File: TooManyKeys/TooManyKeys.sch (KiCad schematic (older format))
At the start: 16 parts

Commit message: Matrix sch finished
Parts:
- R?: value 1k -> 10k
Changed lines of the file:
@@
 $Descr A4 11693 8268
 encoding utf-8
-Sheet 1 1
+Sheet 1 2
 Title ""
 Date ""
@@
 P 1550 3200
 F 0 "R?" V 1354 3200 50  0000 C CNN
-F 1 "1k" V 1445 3200 50  0000 C CNN
+F 1 "10k" V 1445 3200 50  0000 C CNN
 F 2 "" H 1550 3200 50  0001 C CNN
 F 3 "~" H 1550 3200 50  0001 C CNN
@@
 Wire Wire Line
 	2500 4900 2900 4900
+$Sheet
+S 1850 6650 1100 550
+U 5E8A6E89
+F0 "Matrix" 50
+F1 "Matrix.sch" 50
+$EndSheet
 $EndSCHEMATC

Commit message: adding voltage controller and i2c controller
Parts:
- removed F?: 500mA, symbol Device:Polyfuse
- removed USB?: Molex-0548190589, symbol random-keyboard-parts:Molex-0548190589
- added C? (x4): 1uF, Capacitors_SMD:C_0603, symbol Device:C_Small
- added C? (x3): 2.2uF, symbol Device:C_Small
- added C?: 10uF, symbol Device:C_Small
- added C?: 22uF, symbol Device:C_Small
- added F?: 500mA, symbol Device:Polyfuse
- added J?: 54104-3031_Oled, 5051103091, symbol SamacSys_Parts:505110-3091_Oled
- added R? (x2): 5.1k, symbol Device:R_Small
- added R?: 560K, symbol Device:R_Small
- added R? (x2): 4.7k, symbol Device:R_Small
- added R?: 200k, symbol Device:R_Small
- added U?: PRTR5V0U2X, symbol random-keyboard-parts:PRTR5V0U2X
- added U?: PCA9306, symbol Interface:PCA9306
- added U?: AP1117-33, Package_TO_SOT_SMD:SOT-223-3_TabPin2, symbol Regulator_Linear:AP1117-33
- added USB?: HRO-TYPE-C-31-M-12, symbol Type-C:HRO-TYPE-C-31-M-12
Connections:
- net labels added: +3.3V, COL00, COL01, COL02, COL03, COL04, COL05, COL06, COL07, COL08, COL09, COL10, COL11, COL12, COL13, COL14, COL15, COL16, COL17, COL18, COL19, COL20, COL21, COL22, COL23, LED, RESET, ROW0, ROW1, ROW2, ROW3, ROW4, ROW5, ROW6, ROW7, SCL, SCL_3.3, SDA, SDA_3.3
- wire segments 43 -> 166
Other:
- moved on the sheet: C?, R?, SW?, Y?

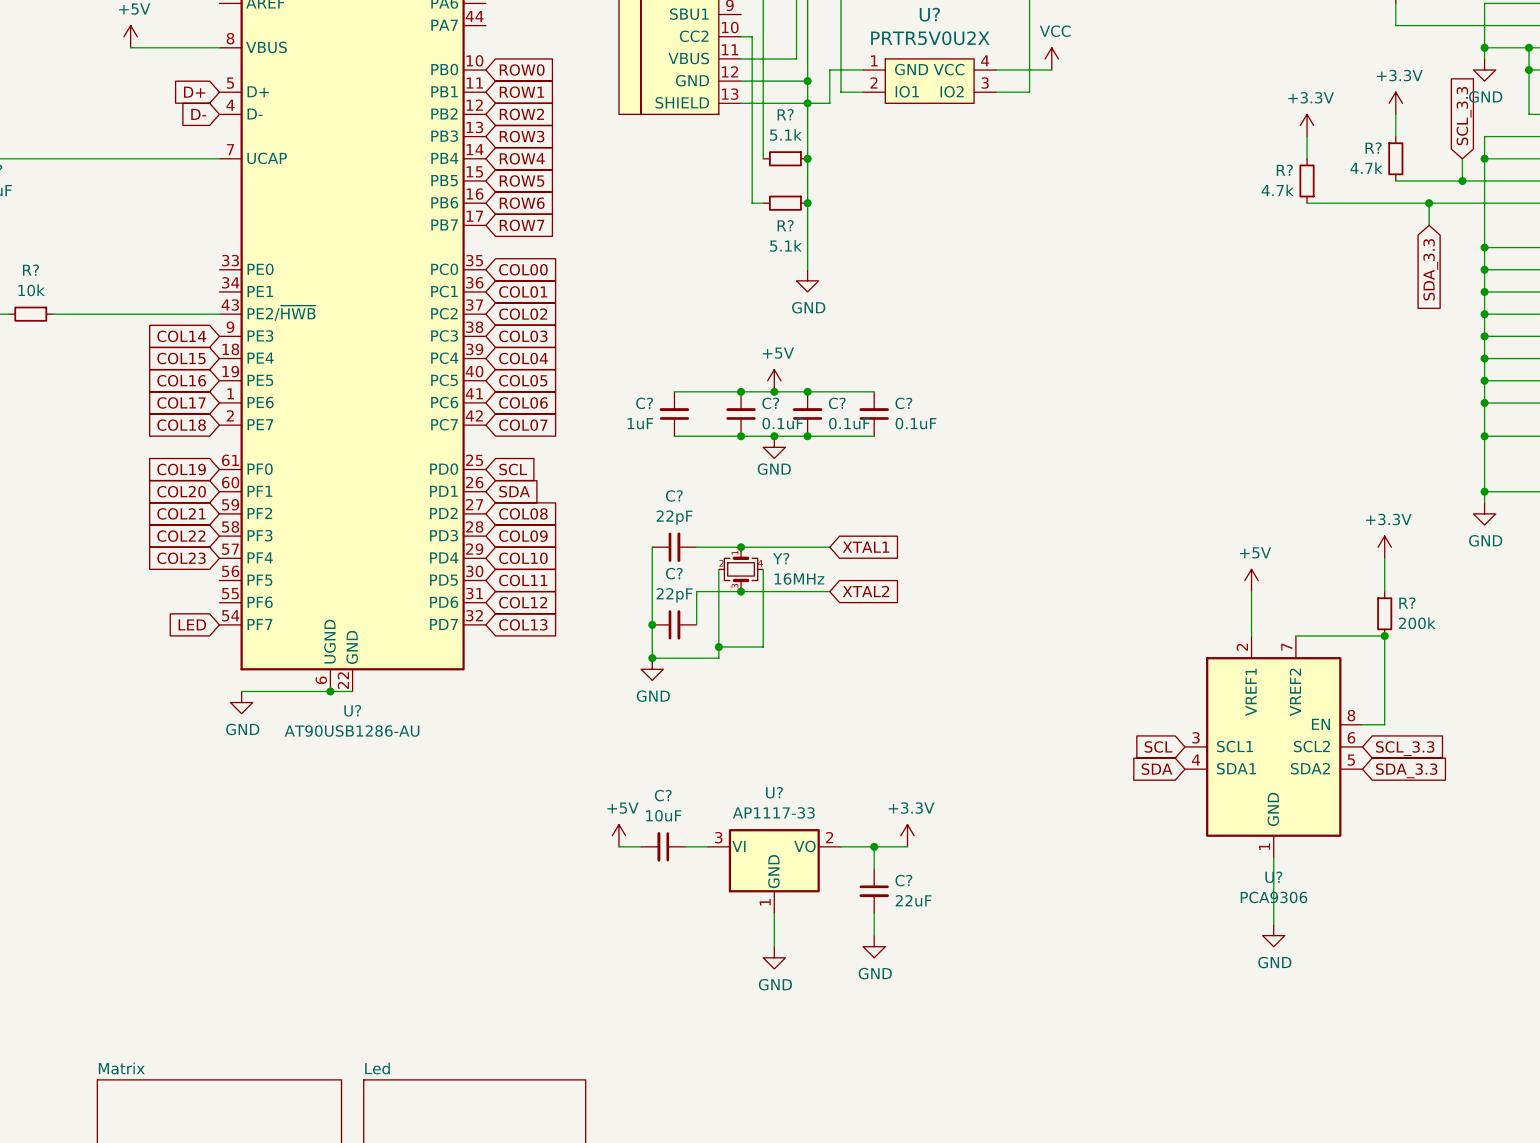
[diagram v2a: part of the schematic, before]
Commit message: adding IS31FL3733-TQ to led sch
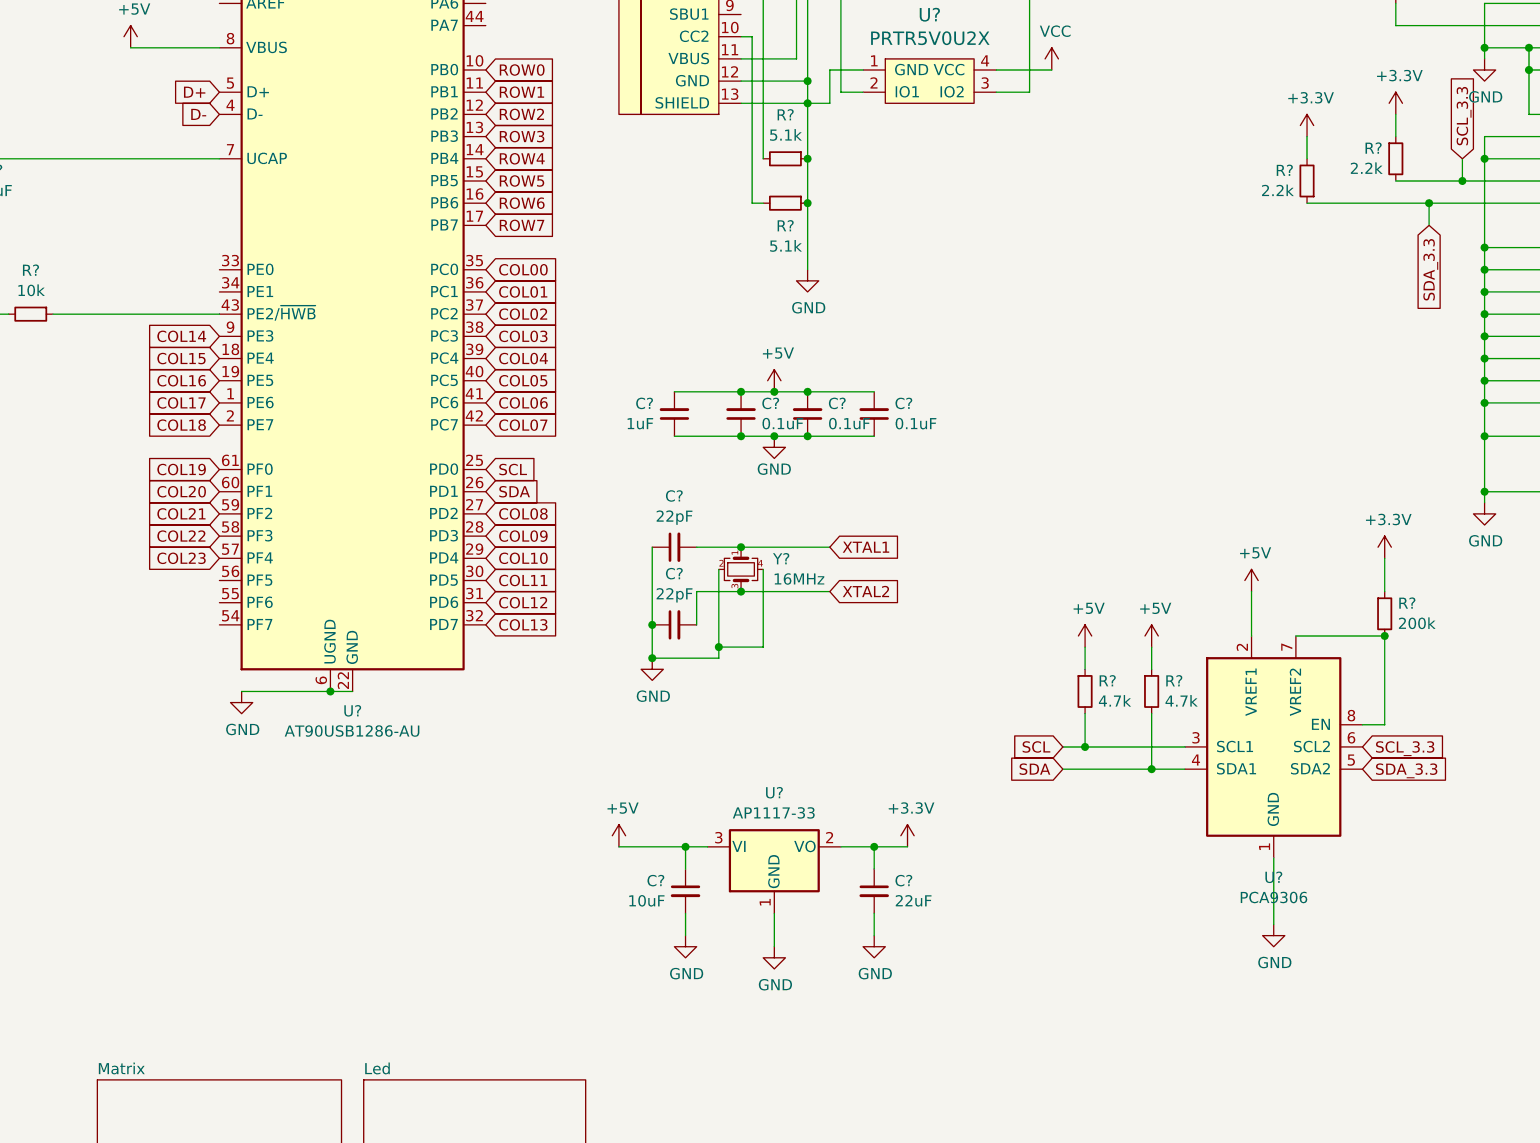
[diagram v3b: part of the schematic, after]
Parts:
- added R? (x2): 4.7k, symbol Device:R_Small
- R? (x2): value 4.7k -> 2.2k
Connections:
- net +5V: now also C?.1, U?.3 (VI), R?.1, R?.1; no longer C?.2
- net GND: now also C?.2
- net SCL: now also R?.2
- net SDA: now also R?.2
- net LED: no longer names the net of U?.54 (PF7)
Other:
- moved on the sheet: C?
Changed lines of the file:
@@
 P 7700 2500
 F 0 "R?" H 7641 2546 50  0000 R CNN
-F 1 "4.7k" H 7641 2455 50  0000 R CNN
+F 1 "2.2k" H 7641 2455 50  0000 R CNN
 F 2 "" H 7700 2500 50  0001 C CNN
 F 3 "~" H 7700 2500 50  0001 C CNN
@@
 P 7300 2600
 F 0 "R?" H 7359 2554 50  0000 L CNN
-F 1 "4.7k" H 7359 2645 50  0000 L CNN
+F 1 "2.2k" H 7359 2645 50  0000 L CNN
 F 2 "" H 7300 2600 50  0001 C CNN
 F 3 "~" H 7300 2600 50  0001 C CNN
@@
 Text GLabel 3600 4000 2    50   Input ~ 0
 SDA
-Text GLabel 2400 4600 0    50   Input ~ 0
-LED
 Text GLabel 3600 2200 2    50   Input ~ 0
 ROW1
@@
 L Device:C_Small C?
 U 1 1 6067D857
-P 4400 5600
-F 0 "C?" V 4171 5600 50  0000 C CNN
-F 1 "10uF" V 4262 5600 50  0000 C CNN
-F 2 "" H 4400 5600 50  0001 C CNN
-F 3 "~" H 4400 5600 50  0001 C CNN
-	1    4400 5600
-	0    1    1    0
-$EndComp
-Wire Wire Line
-	4200 5600 4300 5600
-Wire Wire Line
-	4500 5600 4600 5600
+P 4500 5800
+F 0 "C?" H 4409 5846 50  0000 R CNN
+F 1 "10uF" H 4409 5755 50  0000 R CNN
+F 2 "" H 4500 5800 50  0001 C CNN
+F 3 "~" H 4500 5800 50  0001 C CNN
+	1    4500 5800
+	1    0    0    -1
+$EndComp
 Wire Wire Line
 	4900 5900 4900 6050
@@
 Wire Wire Line
 	7150 5650 7150 5950
-Text GLabel 6750 5150 0    50   Input ~ 0
+Text GLabel 6200 5150 0    50   Input ~ 0
 SCL
-Text GLabel 6750 5250 0    50   Input ~ 0
+Text GLabel 6200 5250 0    50   Input ~ 0
 SDA
 Text GLabel 7550 5150 2    50   Input ~ 0
@@
 	7650 5050 7650 4650
 Connection ~ 7650 4650
+$Comp
+L power:GND #PWR?
+U 1 1 5E863DA2
+P 4500 6000
+F 0 "#PWR?" H 4500 5750 50  0001 C CNN
+F 1 "GND" H 4505 5827 50  0000 C CNN
+F 2 "" H 4500 6000 50  0001 C CNN
+F 3 "" H 4500 6000 50  0001 C CNN
+	1    4500 6000
+	1    0    0    -1
+$EndComp
+Wire Wire Line
+	4200 5600 4500 5600
+Wire Wire Line
+	4500 5700 4500 5600
+Connection ~ 4500 5600
+Wire Wire Line
+	4500 5600 4600 5600
+Wire Wire Line
+	4500 6000 4500 5900
+$Comp
+L power:+5V #PWR?
+U 1 1 5E87C819
+P 6300 4700
+F 0 "#PWR?" H 6300 4550 50  0001 C CNN
+F 1 "+5V" H 6315 4873 50  0000 C CNN
+F 2 "" H 6300 4700 50  0001 C CNN
+F 3 "" H 6300 4700 50  0001 C CNN
+	1    6300 4700
+	1    0    0    -1
+$EndComp
+$Comp
+L power:+5V #PWR?
+U 1 1 5E87D2D2
+P 6600 4700
+F 0 "#PWR?" H 6600 4550 50  0001 C CNN
+F 1 "+5V" H 6615 4873 50  0000 C CNN
+F 2 "" H 6600 4700 50  0001 C CNN
+F 3 "" H 6600 4700 50  0001 C CNN
+	1    6600 4700
+	1    0    0    -1
+$EndComp
+$Comp
+L Device:R_Small R?
+U 1 1 5E87DDE7
+P 6600 4900
+F 0 "R?" H 6659 4946 50  0000 L CNN
+F 1 "4.7k" H 6659 4855 50  0000 L CNN
+F 2 "" H 6600 4900 50  0001 C CNN
+F 3 "~" H 6600 4900 50  0001 C CNN
+	1    6600 4900
+	1    0    0    -1
+$EndComp
+$Comp
+L Device:R_Small R?
+U 1 1 5E87E77F
+P 6300 4900
+F 0 "R?" H 6359 4946 50  0000 L CNN
+F 1 "4.7k" H 6359 4855 50  0000 L CNN
+F 2 "" H 6300 4900 50  0001 C CNN
+F 3 "~" H 6300 4900 50  0001 C CNN
+	1    6300 4900
+	1    0    0    -1
+$EndComp
+Wire Wire Line
+	6200 5150 6300 5150
+Wire Wire Line
+	6300 5000 6300 5150
+Connection ~ 6300 5150
+Wire Wire Line
+	6300 5150 6750 5150
+Wire Wire Line
+	6300 4800 6300 4700
+Wire Wire Line
+	6200 5250 6600 5250
+Wire Wire Line
+	6600 5000 6600 5250
+Connection ~ 6600 5250
+Wire Wire Line
+	6600 5250 6750 5250
+Wire Wire Line
+	6600 4800 6600 4700
 $EndSCHEMATC

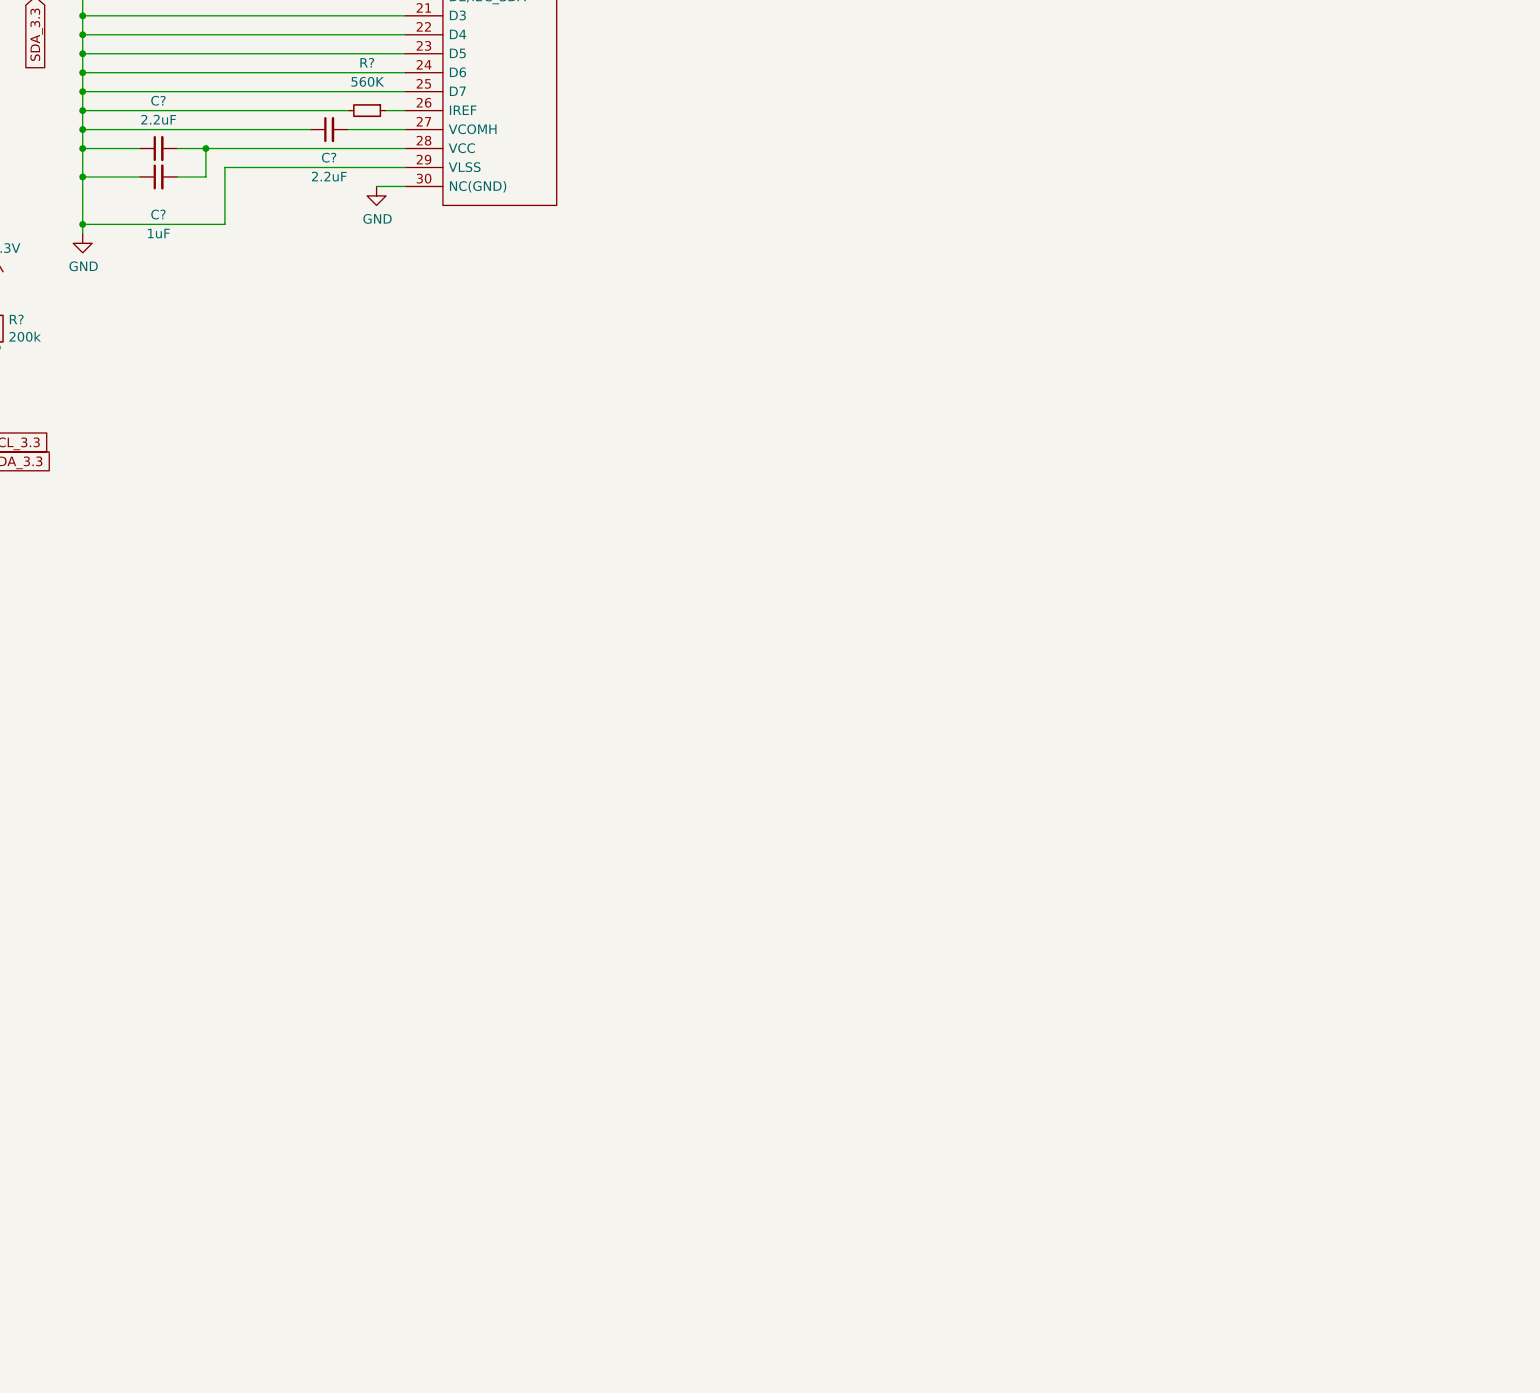
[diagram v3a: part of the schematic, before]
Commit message: Adding led matrix
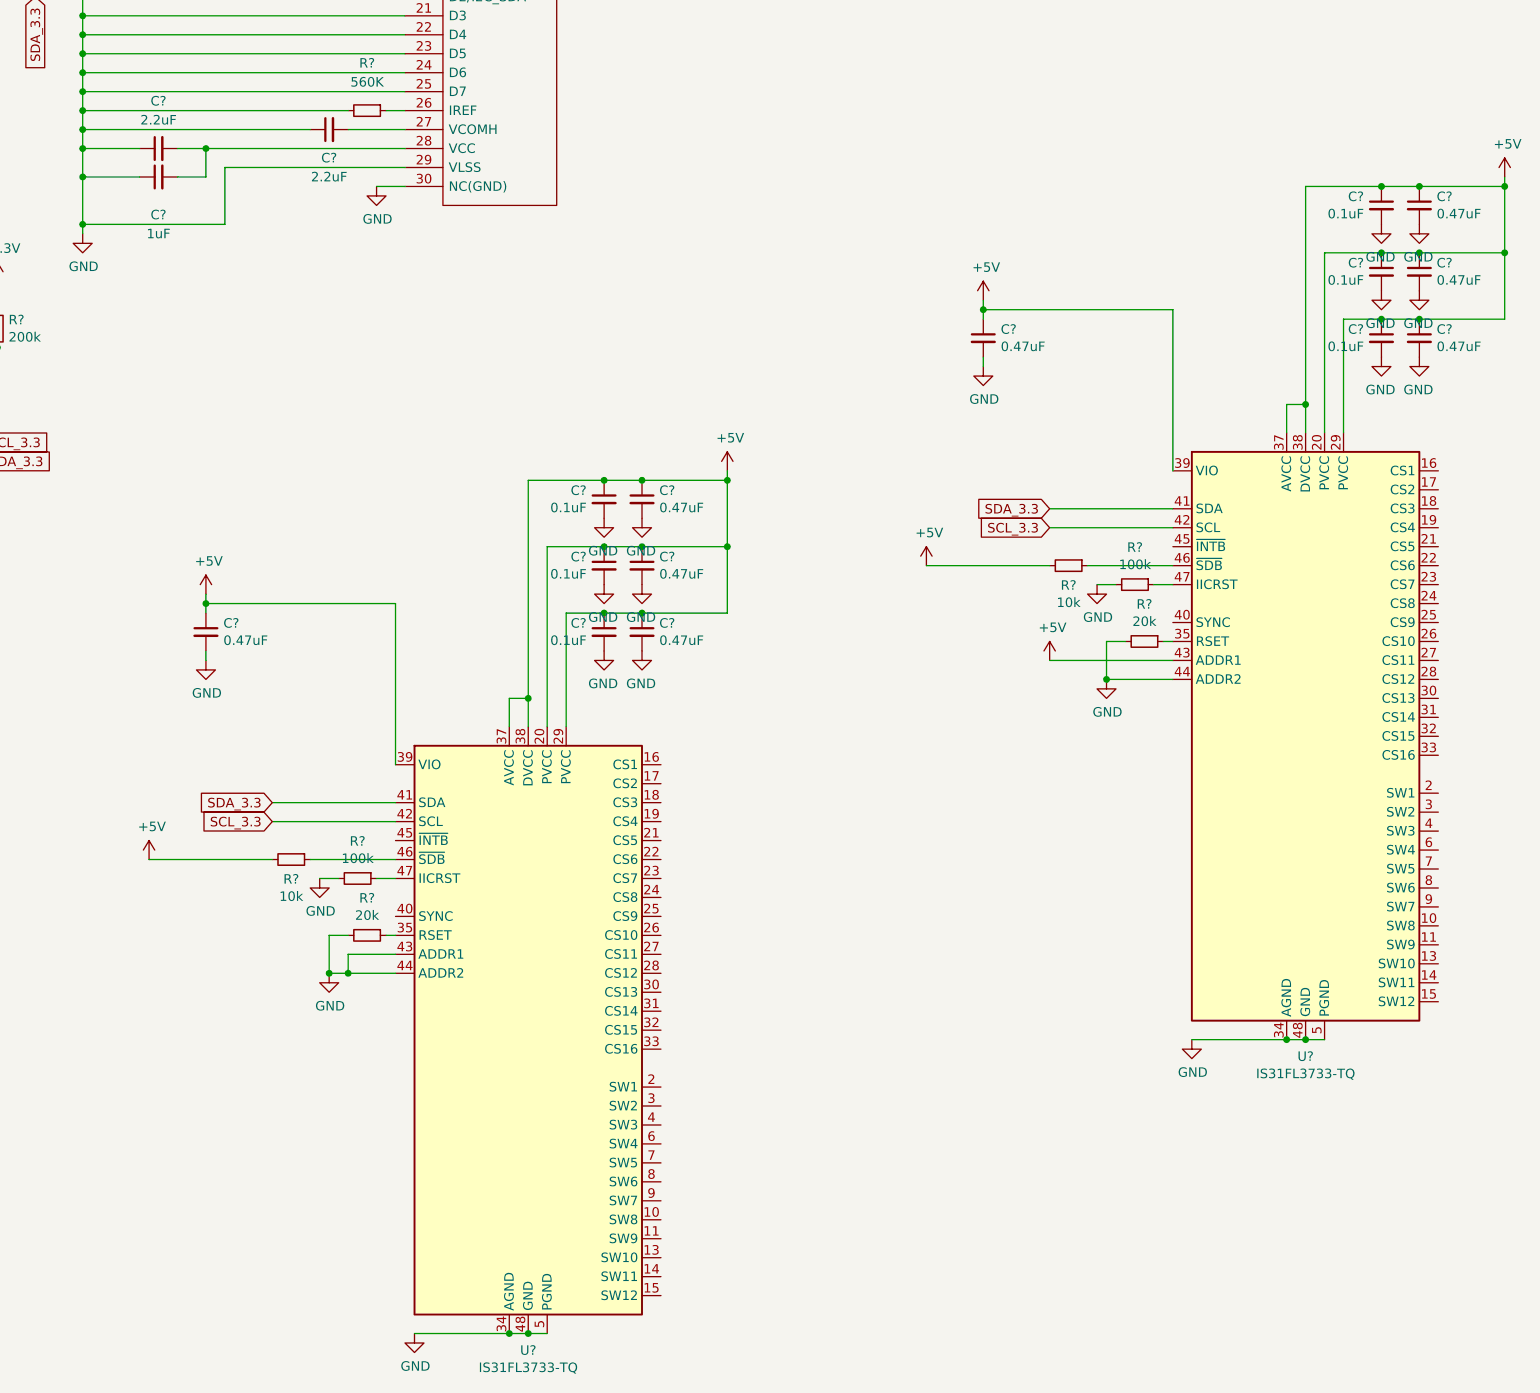
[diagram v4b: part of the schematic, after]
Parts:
- added C? (x8): 0.47uF, symbol Device:C_Small
- added C? (x6): 0.1uF, symbol Device:C_Small
- added MASTER_U?, SLAVE_U?: IS31FL3733-TQ, Package_QFP:TQFP-48-1EP_7x7mm_P0.5mm_EP5x5mm, symbol Driver_LED:IS31FL3733-TQ
- added R? (x2): 100k, symbol Device:R_Small
- added R? (x2): 20k, symbol Device:R_Small
- added R? (x2): 10k, symbol Device:R_Small
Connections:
- net +5V: now also C?.1, C?.1, C?.1, C?.1, C?.1, C?.1, C?.1, C?.1, C?.1, C?.1, C?.1, C?.1, C?.1, C?.1, MASTER_U?.20 (PVCC), MASTER_U?.29 (PVCC), MASTER_U?.37 (AVCC), MASTER_U?.38 (DVCC), MASTER_U?.39 (VIO), R?.2, R?.2, SLAVE_U?.20 (PVCC), SLAVE_U?.29 (PVCC), SLAVE_U?.37 (AVCC), SLAVE_U?.38 (DVCC), SLAVE_U?.39 (VIO), SLAVE_U?.43 (ADDR1)
- net GND: now also C?.2, C?.2, C?.2, C?.2, C?.2, C?.2, C?.2, C?.2, C?.2, C?.2, C?.2, C?.2, C?.2, C?.2, MASTER_U?.12 (PGND), MASTER_U?.34 (AGND), MASTER_U?.43 (ADDR1), MASTER_U?.44 (ADDR2), MASTER_U?.48 (GND), MASTER_U?.49 (GND), MASTER_U?.5 (PGND), R?.2, R?.2, R?.2, R?.2, SLAVE_U?.12 (PGND), SLAVE_U?.34 (AGND), SLAVE_U?.44 (ADDR2), SLAVE_U?.48 (GND), SLAVE_U?.49 (GND), SLAVE_U?.5 (PGND)
- net SCL_3.3: now also MASTER_U?.42 (SCL), SLAVE_U?.42 (SCL)
- net SDA_3.3: now also MASTER_U?.41 (SDA), SLAVE_U?.41 (SDA)
- new net: MASTER_U?.35 (RSET), R?.1
- new net: MASTER_U?.46 (~SDB), R?.1
- new net: MASTER_U?.47 (IICRST), R?.1
- new net: R?.1, SLAVE_U?.35 (RSET)
- new net: R?.1, SLAVE_U?.46 (~SDB)
- new net: R?.1, SLAVE_U?.47 (IICRST)
